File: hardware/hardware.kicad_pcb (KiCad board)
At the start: 2 copper layers, 100 x 100 mm, 44 parts, among them J1 USB_B_Micro, J10 Conn_01x04_Pin, J11 Conn_Coaxial, J2 Conn_02x04_Odd_Even, J5 Conn_01x02, J9 Conn_01x05_Pin, Q1 BSS138, Q2 BSS138, U1 ESP32-WROOM-32, U2 COM-09032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

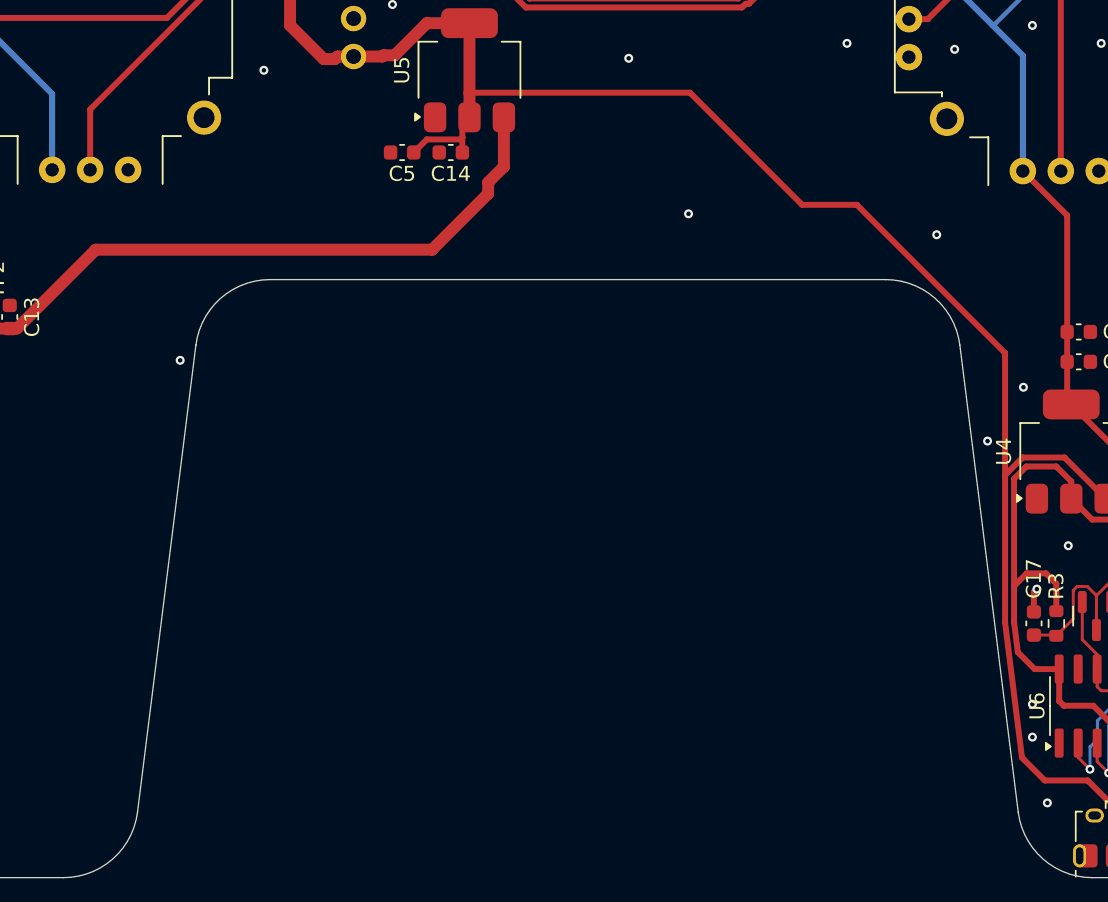
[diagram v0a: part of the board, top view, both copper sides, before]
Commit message: update pcb size
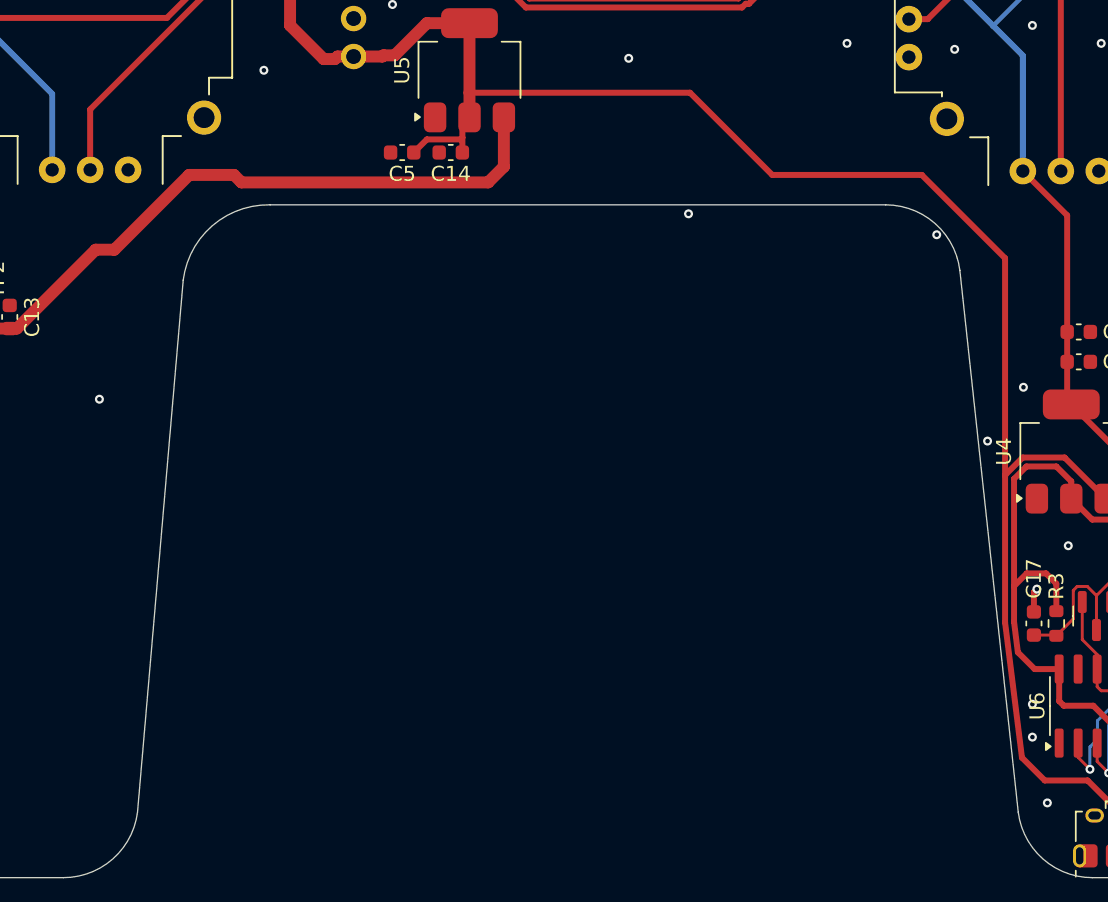
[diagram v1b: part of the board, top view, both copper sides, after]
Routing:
- net +5V: track 150.5 -> 154.2 mm
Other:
- outline, holes or cut-outs redrawn
